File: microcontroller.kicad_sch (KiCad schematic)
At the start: 0 parts

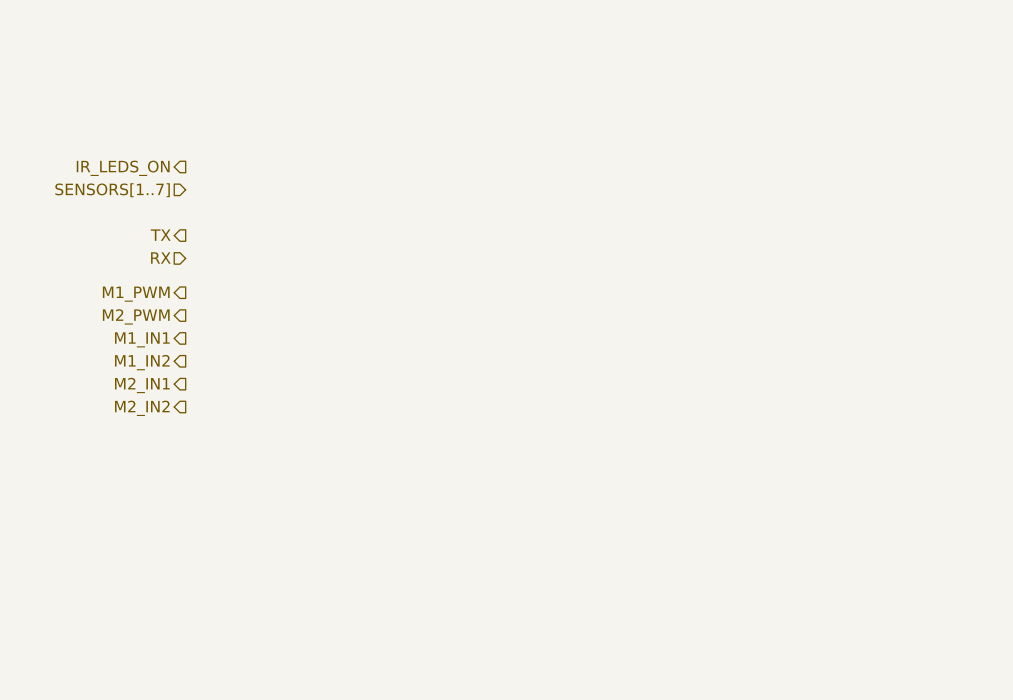
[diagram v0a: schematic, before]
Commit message: Initial microcontroller schematic
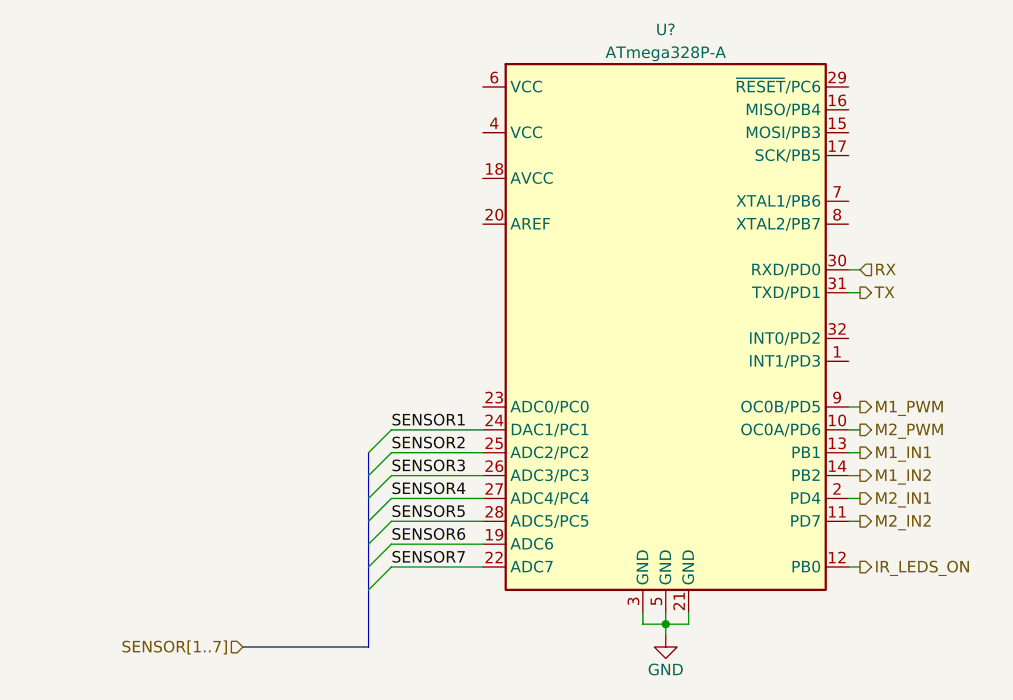
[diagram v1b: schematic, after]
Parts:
- added U?: ATmega328P-A, Package_QFP:TQFP-32_7x7mm_P0.8mm, symbol MCU_Microchip_ATmega:ATmega328P-A
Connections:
- net IR_LEDS_ON: now also U?.12 (PB0)
- net M1_IN1: now also U?.13 (PB1)
- net M1_IN2: now also U?.14 (PB2)
- net M1_PWM: now also U?.9 (OC0B/PD5)
- net M2_IN1: now also U?.2 (PD4)
- net M2_IN2: now also U?.11 (PD7)
- net M2_PWM: now also U?.10 (OC0A/PD6)
- net RX: now also U?.30 (RXD/PD0)
- net TX: now also U?.31 (TXD/PD1)
- new net GND: U?.21 (GND), U?.3 (GND), U?.5 (GND)
- new net SENSOR1: U?.24 (DAC1/PC1)
- new net SENSOR2: U?.25 (ADC2/PC2)
- new net SENSOR3: U?.26 (ADC3/PC3)
- new net SENSOR4: U?.27 (ADC4/PC4)
- new net SENSOR5: U?.28 (ADC5/PC5)
- new net SENSOR6: U?.19 (ADC6)
- new net SENSOR7: U?.22 (ADC7)
